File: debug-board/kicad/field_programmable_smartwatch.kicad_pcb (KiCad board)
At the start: 4 copper layers, 35 x 39 mm, 40 parts, among them IC1 BQ24040DSQR, IC2 STM32WB55CEU6, J1 SPI_Header, J2 LPUART_Header, J3 DX07S016JA1R1500, J4 GPIO_Header, Q1 Q_PMOS_DGS, SW2 SW_DIP_x01, Y1 32M, Y2 32.768k

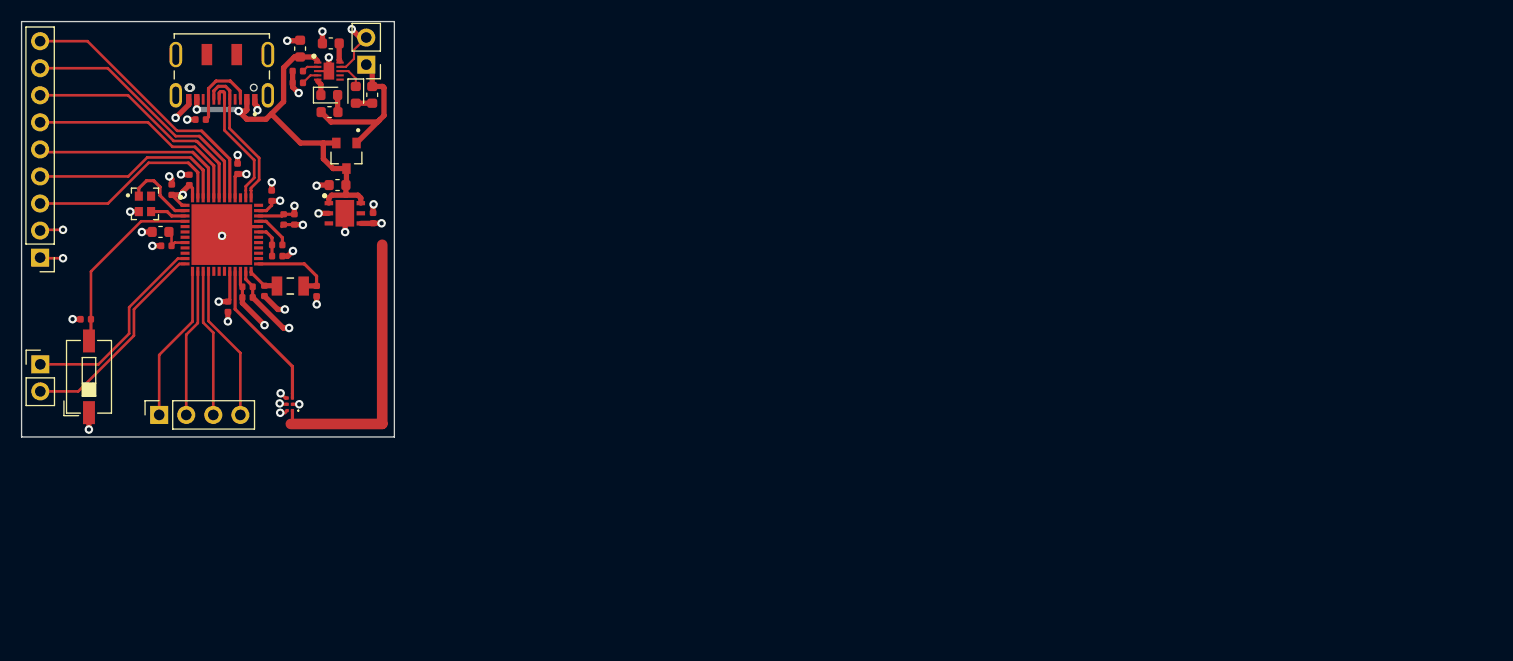
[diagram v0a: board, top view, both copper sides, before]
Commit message: Reworking debug board design
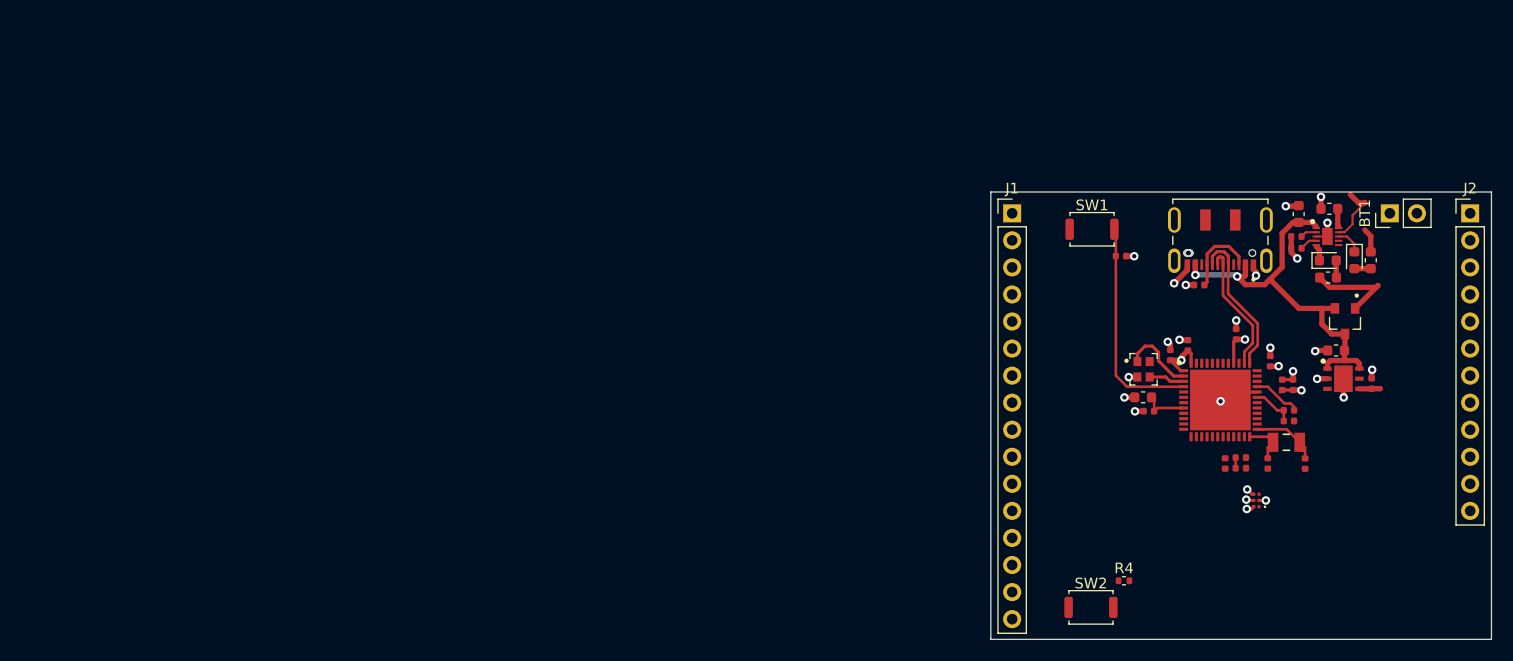
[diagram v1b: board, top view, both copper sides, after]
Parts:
- removed J4: GPIO_Header, Connector_PinHeader_2.54mm:PinHeader_1x09_P2.54mm_Vertical
- added R4: 100k, Resistor_SMD:R_0402_1005Metric, F.Cu at (143.5, 103.5)
- added SW1: SW_Push, Button_Switch_SMD:SW_Push_SPST_NO_Alps_SKRK, F.Cu at (140.5, 70.5)
- J1: value SPI_Header -> Conn_01x16_Male; footprint Connector_PinSocket_2.54mm:PinSocket_1x04_P2.54mm_Vertical -> Connector_PinHeader_2.54mm:PinHeader_1x16_P2.54mm_Vertical
- J2: value LPUART_Header -> Conn_01x12_Male; footprint Connector_PinHeader_2.54mm:PinHeader_1x02_P2.54mm_Vertical -> Connector_PinHeader_2.54mm:PinHeader_1x12_P2.54mm_Vertical
- SW2: value SW_DIP_x01 -> SW_Push; footprint Button_Switch_SMD:SW_DIP_SPSTx01_Slide_6.7x4.1mm_W6.73mm_P2.54mm_LowProfile_JPin -> Button_Switch_SMD:SW_Push_SPST_NO_Alps_SKRK
- moved J2 135.0 mm to (176.0, 69.0)
- moved R7 97.4 mm to (143.2, 73.0), turned to 0 degrees
- moved BT1 97.1 mm to (168.5, 69.0), turned to 90 degrees
- moved SW2 96.5 mm to (140.4, 106.0), turned to 0 degrees
- moved L1 96.2 mm to (159.0, 87.5)
- moved C11 96.2 mm to (159.0, 88.5)
- moved C18 95.6 mm to (157.0, 92.5)
- moved C17 95.0 mm to (159.4, 85.1)
- moved C19 95.0 mm to (158.4, 85.1)
- moved IC2 95.0 mm to (152.6, 86.5)
- moved J3 95.0 mm to (152.6, 72.7)
- moved C1 95.0 mm to (159.9, 69.1)
- moved C10 95.0 mm to (154.0, 80.4)
- moved C20 95.0 mm to (163.4, 81.9)
- moved C21 95.0 mm to (166.8, 85.0)
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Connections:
- IC2 pad 10: Net-(IC2-Pad10) -> /PA1
- IC2 pad 17: Net-(IC2-Pad17) -> /PA8
- IC2 pad 18: Net-(IC2-Pad18) -> /PA9
- IC2 pad 19: Net-(IC2-Pad19) -> /PB2
- IC2 pad 28: Net-(IC2-Pad28) -> /PB0
- IC2 pad 29: Net-(IC2-Pad29) -> /PB1
- IC2 pad 36: Net-(IC2-Pad36) -> /PA10
- IC2 pad 39: Net-(IC2-Pad39) -> /PA13
- IC2 pad 5: Net-(IC2-Pad5) -> /PB8
- IC2 pad 6: Net-(IC2-Pad6) -> /PB9
- IC2 pad 7: Net-(IC2-Pad7) -> /RESET
- IC2 pad 9: Net-(IC2-Pad9) -> /PA0
- J1 pad 1: /NSS -> /PA0
- J1 pad 2: /SCK -> /PA1
- J1 pad 3: /MISO -> /LPUART_TX
- J1 pad 4: /MOSI -> /LPUART_RX
- J2 pad 1: /LPUART_TX -> +3V3
- J2 pad 2: /LPUART_RX -> GND
- SW2 pad 2: /BOOT0 -> /RESET
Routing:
- net Net-(AE1-Pad1): track 27.1 -> 0.00 mm
- net /PA14: track 26.0 -> 0.00 mm
- net /PA15: track 24.4 -> 0.00 mm
- net /PB3: track 22.7 -> 0.00 mm
- net /PB4: track 21.0 -> 0.00 mm
- net /LPUART_RX: track 20.0 -> 0.00 mm
- net /PB5: track 19.3 -> 0.00 mm
- net /PB7: track 19.2 -> 0.00 mm
- net /LPUART_TX: track 19.2 -> 0.00 mm
- net +3V3: track 33.1 -> 14.0 mm, vias 10 -> 5
- net /PB6: track 19.1 -> 0.00 mm
- net /NSS: track 14.8 -> 0.00 mm
- net /MOSI: track 14.7 -> 0.00 mm
- net /RF1: track 14.1 -> 0.00 mm
- net /SCK: track 13.9 -> 0.00 mm
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- added copper zone on In1.Cu, net +3V3
- added copper zone on In2.Cu, net GND
- removed copper zone on In2.Cu, net +3V3
- removed copper zone on In1.Cu, net GND
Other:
- board size 35 x 39 mm -> 47 x 42 mm
- rule trace_min: 0.2 -> 0.15
- rule via_min_drill: 0.3 -> 0.2
